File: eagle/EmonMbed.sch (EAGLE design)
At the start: 127 parts, among them IC2 74HC595D, IC3 74HC595D, IC4 ADE7758RW, J1 CON_TERMINAL_BLOCK_02-5MM, J2 CON_TERMINAL_BLOCK_02-5MM, J3 CON_TERMINAL_BLOCK_02-5MM, J4 CON_TERMINAL_BLOCK_03-5MM, J7 CON_TERMINAL_BLOCK_02-5MM, Q1 25MHz, U1 STM32L152RBT6, U2 W5500, Y1 32.768kHz, Y2 32.768kHz

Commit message: new schematics and datasheet
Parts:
- added C37: 10uF, rcl:CPOL-USC/6032-28R
- added C38, C39, C40, C41, C42, C43, C44, C55, C56: 0.1uF, rcl:C-USC0805
- added C45, C59: 10uF, rcl:CPOL-US153CLV-0605
- added C46, C60: 0.1uF, rcl:CPOL-US153CLV-0605
- added C47, C48, C49, C50, C51, C52, C53, C54: 100nF, rcl:C-EUC0603
- added D1, D2, D3, D4: 1N4001, diode:DIODE-DO-214AC
- added IC6: REG1117, burr-brown:REG1117
- added IC7: 7805DT, linear:7805DT
- added JP10, JP11: (no value), pinhead:PINHD-1X8
- added JP12, JP13: (no value), pinhead:PINHD-1X3
- added JP14: (no value), pinhead:PINHD-1X2
- added L1: 150Mhz, rcl:L-USWE-TPC
- added R41, R42: R120, resistor:R-EU_R0603
- added R43: 10, SparkFun-Passives:RESISTOR0603-RES
- added SV1: (no value), con-lstb:MA08-1
- added T3, T9: (no value), transistor-neu-to92:MMBT2222ALT1-NPN-SOT23-BEC
- added U$1, U$4: ADUM1402, adum140x:ADUM1402
- added U$3: ESP-07, esp-07:ESP-07
- added X2: (no value), con-ptr500:AK500/2-H
- C23, C24, C25, C26, C27, C28, C33, C34, C35, C36: device SparkFun-Passives:CAPPTH2 -> SparkFun-Passives:CAP0603-CAP
- JP1: value ESP8266 -> Vsel; device pinhead:PINHD-2X4 -> pinhead:PINHD-1X3
- R26, R27, R28, R29, R30, R31, R32, R33, R34, R35, R36, R37, R38: device SparkFun-Passives:RESISTORPTH-1/4W -> SparkFun-Passives:RESISTOR0603-RES
- R4: value 10k -> 10; device resistor:R-US_R0603 -> SparkFun-Passives:RESISTOR0603-RES
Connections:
- removed net CS: JP2.7
- removed net PA0: U1.PA0-WKUP1
- removed net PA1: U1.PA1
- removed net PA10: U1.PA10
- removed net PA11: U1.PA11
- removed net PA12: U1.PA12
- removed net PA15: U1.PA15
- removed net PA4: U1.PA4
- removed net PA8: U1.PA8
- removed net PA9: U1.PA9
- removed net PB0: U1.PB0
- removed net PB1: U1.PB1
- removed net PB12: U1.PB12
- removed net PB13: U1.PB13
- removed net PB14: U1.PB14
- removed net PB15: U1.PB15
- removed net PB4: U1.PB4
- removed net PB5: U1.PB5
- removed net PB7: U1.PB7
- removed net PC10: U1.PC10
- removed net PC11: U1.PC11
- removed net PC12: U1.PC12
- removed net PC4: U1.PC4
- removed net PC5: U1.PC5
- removed net PC6: U1.PC6
- removed net PC7: U1.PC7
- removed net PC8: U1.PC8
- removed net PC9: U1.PC9
- removed net PD2: U1.PD2
- removed net SCLK: U2.SCLK
- removed net SCSN: R8.1, U2.SCS_N
- removed net SDI(MOSI): JP2.4
- removed net SDO(MISO): JP2.1
- removed net SPI_CS: U1.PB6
- removed net SPI_MISO: U1.PA6
- removed net SPI_MOSI: U1.PA7
- removed net SPI_SCK: U1.PA5
- removed net TCK: U1.PA14
- removed net TMS: U1.PA13
- new net !CS: SV1.3
- new net ADE_CS: U$4.VIC, U1.PA12
- new net ADE_MISO: U$1.VOB, U1.PA14
- new net ADE_MOSI: U$1.VID, U1.PA15
- new net ADE_SCK: U$1.VIC, U1.PA13
- new net APCF: U$1.VOA, U1.PB4
- new net AVADE: C44.1, IC4.PWR.AVDD, R4.2
- new net DGND1: C51.2, C52.2
- new net ESP_GPIO0: JP13.2, U$3.GPIO0
- new net ESP_RX: JP14.1, U$3.URXD, U1.PC12
- new net ESP_TX: JP14.2, U$3.UTXD, U1.PD2
- new net ETH_CS: R8.1, U1.PA4, U2.SCS_N
- new net ETH_MISO: U1.PA6, U2.MISO
- new net ETH_MOSI: U1.PA7, U2.MOSI
- new net ETH_SCK: U1.PA5, U2.SCLK
- new net GESP: C54.2, JP12.2, JP13.3, U$3.GND, U$3.GPIO15
- new net GEXT: JP12.3
- new net IRQ: SV1.7, U$4.VOA, U1.PB6
- new net LCD_CS: JP2.7, U1.PB12
- new net LCD_MISO: JP2.1, U1.PB14
- new net LCD_MOSI: JP2.4, U1.PB15
- new net LCD_SCK: JP2.3, U1.PB13
- new net N$44: R41.2, T9.B
- new net N$45: R42.2, T3.B
- new net PWRKEY: R41.1
- new net VADE: C37.+, C38.1, C39.1, C40.1, C41.1, C42.1, C43.1, C60.+, D3.A, IC4.PWR.DVDD, IC7.VO, R4.1, U$1.VDD1, U$1.VDD2, U$1.VE1, U$1.VE2, U$4.VDD1, U$4.VDD2, U$4.VE1, U$4.VE2
- new net VARCF: U$4.VOB, U1.PB5
- new net VCC1: C51.1, C52.1
- new net VESP: C54.1, JP1.2, JP13.1, U$3.CH_PD, U$3.GPIO2, U$3.VCC
- new net VEXT: JP1.3
- new net VRAW: D1.A, D2.A, X2-1.KL
- net !ADECS: now also U$4.VOC
- net ADEAPCF: now also U$1.VIA
- net ADEIN: now also U$1.VOD
- net ADEIRQ: now also U$4.VIB
- net ADEOUT: now also U$1.VIB
- net ADESCK: now also U$1.VOC
- net ADEVARCF: now also U$4.VIA
- net AGND: now also C44.2, C47.2, C48.2, C49.2, C50.2, C56.2, L1.1
- net BOOT0: no longer R4.2
- net DGND: now also C37.-, C38.2, C39.2, C41.2, C43.2, C45.-, C46.-, C53.2, C55.2, C59.-, C60.-, IC6.GND, IC7.GND, JP12.1, L1.2, T3.E, T9.E, U$1.GND1@1, U$1.GND1@2, U$4.GND1@1, U$4.GND1@2, X2-2.KL; no longer JP1.2, R4.1
- net GND: now also C40.2, C42.2, SV1.2, U$1.GND2@1, U$1.GND2@2, U$4.GND2@1, U$4.GND2@2
- net MISO: now also SV1.6; no longer U2.MISO
- net MOSI: now also SV1.4; no longer U2.MOSI
- net Q1: now also JP10.1
- net Q10: now also JP11.2
- net Q11: now also JP11.3
- net Q12: now also JP11.4
- net Q13: now also JP11.5
- net Q14: now also JP11.6
- net Q15: now also JP11.7
- net Q16: now also JP11.8
- net Q2: now also JP10.2
- net Q3: now also JP10.3
- net Q4: now also JP10.4
- net Q5: now also JP10.5
- net Q6: now also JP10.6
- net Q7: now also JP10.7
- net Q8: now also JP10.8
- net Q9: now also JP11.1
- net RESET: now also R42.1
- net SCK: now also SV1.5; no longer JP2.3
- net SERIAL_RX: now also U1.PA10; no longer JP1.1, U1.PA3
- net SERIAL_TX: now also U1.PA9; no longer JP1.8, U1.PA2
- net SIM_PWRKEY: now also T9.C, U1.PC4
- net SIM_RESET: now also T3.C, U1.PC5
- net SIM_RX: now also U1.PC10
- net SIM_TX: now also U1.PC11
- net VCC: now also C47.1, C48.1, C49.1, C50.1, C56.1, R43.2, SV1.8; no longer IC4.PWR.AVDD
- net VDD: now also C46.+, C53.1, C55.1, D4.A, IC6.VOUT, JP1.1, R43.1; no longer IC4.PWR.DVDD, JP1.3, JP1.7
- net VIN: now also C45.+, C59.+, D1.C, D2.C, D3.C, D4.C, IC6.VIN, IC7.VI
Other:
- note added: "LMS8117A"
- moved on the sheet: C1, C10, C10-4U7, C11, C11-22P, C12, C13, C14, C15, C16, C17, C18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

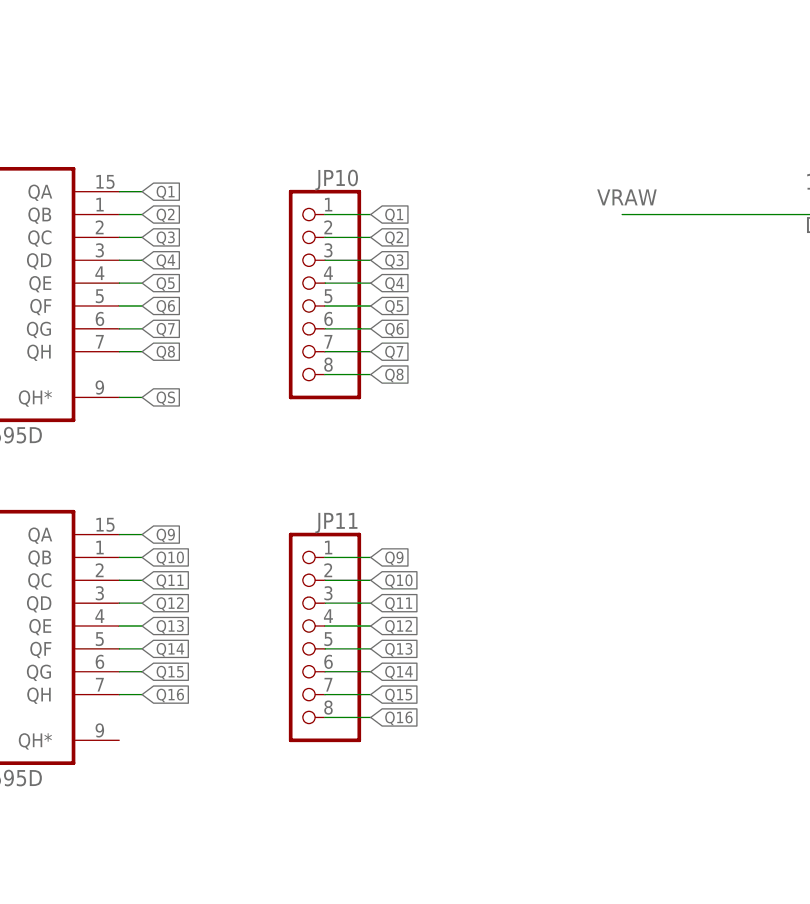
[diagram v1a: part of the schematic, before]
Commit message: update schematic
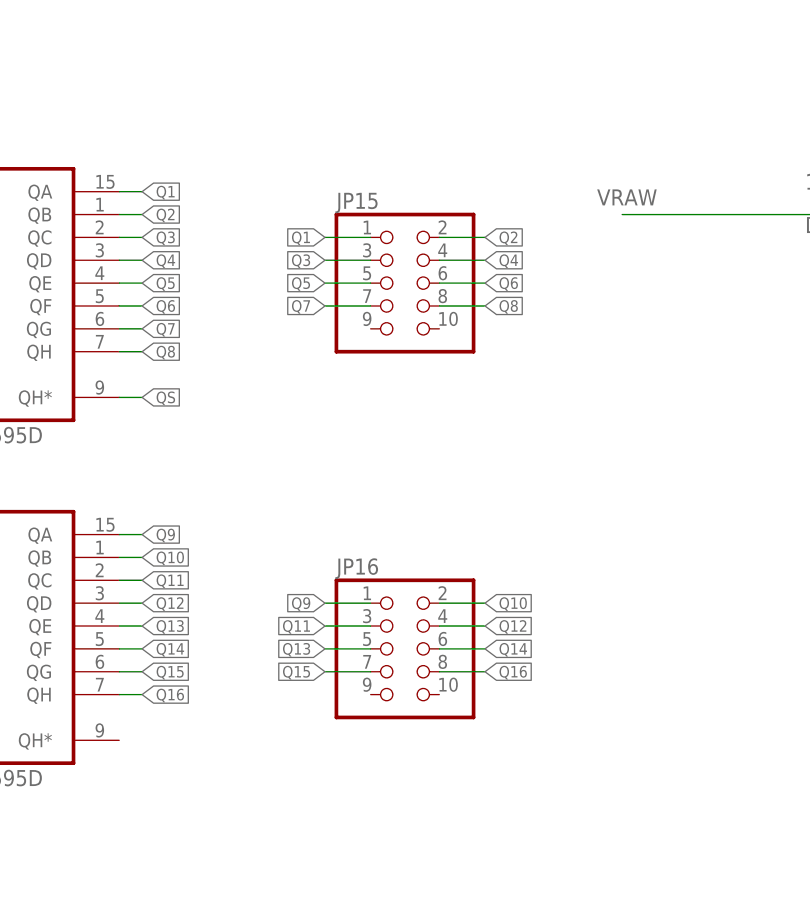
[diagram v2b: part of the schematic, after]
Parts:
- removed JP10, JP11: (no value), pinhead:PINHD-1X8
- added JP15, JP16: (no value), pinhead:PINHD-2X5/90
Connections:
- net Q1: now also JP15.1; no longer JP10.1
- net Q10: now also JP16.2; no longer JP11.2
- net Q11: now also JP16.3; no longer JP11.3
- net Q12: now also JP16.4; no longer JP11.4
- net Q13: now also JP16.5; no longer JP11.5
- net Q14: now also JP16.6; no longer JP11.6
- net Q15: now also JP16.7; no longer JP11.7
- net Q16: now also JP16.8; no longer JP11.8
- net Q2: now also JP15.2; no longer JP10.2
- net Q3: now also JP15.3; no longer JP10.3
- net Q4: now also JP15.4; no longer JP10.4
- net Q5: now also JP15.5; no longer JP10.5
- net Q6: now also JP15.6; no longer JP10.6
- net Q7: now also JP15.7; no longer JP10.7
- net Q8: now also JP15.8; no longer JP10.8
- net Q9: now also JP16.1; no longer JP11.1
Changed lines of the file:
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@@
 <part name="R40" library="resistor" deviceset="R-US_" device="R0603" value="10k"/>
 <part name="JP9" library="pinhead" deviceset="PINHD-1X4" device="" value="USART"/>
-<part name="JP10" library="pinhead" deviceset="PINHD-1X8" device=""/>
-<part name="JP11" library="pinhead" deviceset="PINHD-1X8" device=""/>
 <part name="U$3" library="esp-07" deviceset="ESP-07" device=""/>
 <part name="JP1" library="pinhead" deviceset="PINHD-1X3" device="" value="Vsel"/>
@@
 <part name="C45" library="rcl" deviceset="CPOL-US" device="153CLV-0605" value="10uF"/>
 <part name="C46" library="rcl" deviceset="CPOL-US" device="153CLV-0605" value="0.1uF"/>
+<part name="JP15" library="pinhead" deviceset="PINHD-2X5" device="/90"/>
+<part name="JP16" library="pinhead" deviceset="PINHD-2X5" device="/90"/>
 </parts>
 <sheets>
@@
 <instance part="R40" gate="G$1" x="132.08" y="187.96"/>
 <instance part="JP9" gate="A" x="177.8" y="160.02"/>
-<instance part="JP10" gate="A" x="408.94" y="269.24" rot="MR0"/>
-<instance part="JP11" gate="A" x="408.94" y="231.14" rot="MR0"/>
 <instance part="U$3" gate="G$1" x="386.08" y="330.2"/>
 <instance part="JP1" gate="A" x="396.24" y="373.38"/>
@@
 <instance part="C45" gate="G$1" x="477.52" y="271.78"/>
 <instance part="C46" gate="G$1" x="505.46" y="271.78"/>
+<instance part="JP15" gate="A" x="419.1" y="271.78"/>
+<instance part="JP16" gate="A" x="419.1" y="231.14"/>
 </instances>
 <busses>
@@
 </segment>
 <segment>
-<pinref part="JP10" gate="A" pin="8"/>
-<wire x1="416.56" y1="261.62" x2="411.48" y2="261.62" width="0.1524" layer="91"/>
-<label x="416.56" y="261.62" size="1.27" layer="95" xref="yes"/>
+<pinref part="JP15" gate="A" pin="8"/>
+<wire x1="424.18" y1="269.24" x2="429.26" y2="269.24" width="0.1524" layer="91"/>
+<label x="429.26" y="269.24" size="1.27" layer="95" xref="yes"/>
 </segment>
 </net>
@@
 </segment>
 <segment>
-<pinref part="JP10" gate="A" pin="7"/>
-<wire x1="411.48" y1="264.16" x2="416.56" y2="264.16" width="0.1524" layer="91"/>
-<label x="416.56" y="264.16" size="1.27" layer="95" xref="yes"/>
+<pinref part="JP15" gate="A" pin="7"/>
+<wire x1="416.56" y1="269.24" x2="411.48" y2="269.24" width="0.1524" layer="91"/>
+<label x="411.48" y="269.24" size="1.27" layer="95" rot="R180" xref="yes"/>
 </segment>
 </net>
@@
 </segment>
 <segment>
-<pinref part="JP10" gate="A" pin="6"/>
-<wire x1="416.56" y1="266.7" x2="411.48" y2="266.7" width="0.1524" layer="91"/>
-<label x="416.56" y="266.7" size="1.27" layer="95" xref="yes"/>
+<pinref part="JP15" gate="A" pin="6"/>
+<wire x1="429.26" y1="271.78" x2="424.18" y2="271.78" width="0.1524" layer="91"/>
+<label x="429.26" y="271.78" size="1.27" layer="95" xref="yes"/>
 </segment>
 </net>
@@
 </segment>
 <segment>
-<pinref part="JP10" gate="A" pin="5"/>
-<wire x1="411.48" y1="269.24" x2="416.56" y2="269.24" width="0.1524" layer="91"/>
-<label x="416.56" y="269.24" size="1.27" layer="95" xref="yes"/>
+<pinref part="JP15" gate="A" pin="5"/>
+<wire x1="416.56" y1="271.78" x2="411.48" y2="271.78" width="0.1524" layer="91"/>
+<label x="411.48" y="271.78" size="1.27" layer="95" rot="R180" xref="yes"/>
 </segment>
 </net>
@@
 </segment>
 <segment>
-<pinref part="JP10" gate="A" pin="4"/>
-<wire x1="416.56" y1="271.78" x2="411.48" y2="271.78" width="0.1524" layer="91"/>
-<label x="416.56" y="271.78" size="1.27" layer="95" xref="yes"/>
+<pinref part="JP15" gate="A" pin="4"/>
+<wire x1="424.18" y1="274.32" x2="429.26" y2="274.32" width="0.1524" layer="91"/>
+<label x="429.26" y="274.32" size="1.27" layer="95" xref="yes"/>
 </segment>
 </net>
@@
 </segment>
 <segment>
-<pinref part="JP10" gate="A" pin="3"/>
-<wire x1="411.48" y1="274.32" x2="416.56" y2="274.32" width="0.1524" layer="91"/>
-<label x="416.56" y="274.32" size="1.27" layer="95" xref="yes"/>
+<pinref part="JP15" gate="A" pin="3"/>
+<wire x1="416.56" y1="274.32" x2="411.48" y2="274.32" width="0.1524" layer="91"/>
+<label x="411.48" y="274.32" size="1.27" layer="95" rot="R180" xref="yes"/>
 </segment>
 </net>
@@
 </segment>
 <segment>
-<pinref part="JP10" gate="A" pin="2"/>
-<wire x1="416.56" y1="276.86" x2="411.48" y2="276.86" width="0.1524" layer="91"/>
-<label x="416.56" y="276.86" size="1.27" layer="95" xref="yes"/>
+<pinref part="JP15" gate="A" pin="2"/>
+<wire x1="424.18" y1="276.86" x2="429.26" y2="276.86" width="0.1524" layer="91"/>
+<label x="429.26" y="276.86" size="1.27" layer="95" xref="yes"/>
 </segment>
 </net>
@@
 </segment>
 <segment>
-<pinref part="JP10" gate="A" pin="1"/>
-<wire x1="411.48" y1="279.4" x2="416.56" y2="279.4" width="0.1524" layer="91"/>
-<label x="416.56" y="279.4" size="1.27" layer="95" xref="yes"/>
+<pinref part="JP15" gate="A" pin="1"/>
+<wire x1="416.56" y1="276.86" x2="411.48" y2="276.86" width="0.1524" layer="91"/>
+<label x="411.48" y="276.86" size="1.27" layer="95" rot="R180" xref="yes"/>
 </segment>
 </net>
@@
 </segment>
 <segment>
-<pinref part="JP11" gate="A" pin="8"/>
-<wire x1="416.56" y1="223.52" x2="411.48" y2="223.52" width="0.1524" layer="91"/>
-<label x="416.56" y="223.52" size="1.27" layer="95" xref="yes"/>
+<pinref part="JP16" gate="A" pin="8"/>
+<wire x1="429.26" y1="228.6" x2="424.18" y2="228.6" width="0.1524" layer="91"/>
+<label x="429.26" y="228.6" size="1.27" layer="95" xref="yes"/>
 </segment>
 </net>
@@
 </segment>
 <segment>
-<pinref part="JP11" gate="A" pin="7"/>
-<wire x1="411.48" y1="226.06" x2="416.56" y2="226.06" width="0.1524" layer="91"/>
-<label x="416.56" y="226.06" size="1.27" layer="95" xref="yes"/>
+<pinref part="JP16" gate="A" pin="7"/>
+<wire x1="411.48" y1="228.6" x2="416.56" y2="228.6" width="0.1524" layer="91"/>
+<label x="411.48" y="228.6" size="1.27" layer="95" rot="R180" xref="yes"/>
 </segment>
 </net>
@@
 </segment>
 <segment>
-<pinref part="JP11" gate="A" pin="6"/>
-<wire x1="416.56" y1="228.6" x2="411.48" y2="228.6" width="0.1524" layer="91"/>
-<label x="416.56" y="228.6" size="1.27" layer="95" xref="yes"/>
+<pinref part="JP16" gate="A" pin="6"/>
+<wire x1="424.18" y1="231.14" x2="429.26" y2="231.14" width="0.1524" layer="91"/>
+<label x="429.26" y="231.14" size="1.27" layer="95" xref="yes"/>
 </segment>
 </net>
@@
 </segment>
 <segment>
-<pinref part="JP11" gate="A" pin="5"/>
-<wire x1="411.48" y1="231.14" x2="416.56" y2="231.14" width="0.1524" layer="91"/>
-<label x="416.56" y="231.14" size="1.27" layer="95" xref="yes"/>
+<pinref part="JP16" gate="A" pin="5"/>
+<wire x1="416.56" y1="231.14" x2="411.48" y2="231.14" width="0.1524" layer="91"/>
+<label x="411.48" y="231.14" size="1.27" layer="95" rot="R180" xref="yes"/>
 </segment>
 </net>
@@
 </segment>
 <segment>
-<pinref part="JP11" gate="A" pin="4"/>
-<wire x1="416.56" y1="233.68" x2="411.48" y2="233.68" width="0.1524" layer="91"/>
-<label x="416.56" y="233.68" size="1.27" layer="95" xref="yes"/>
+<pinref part="JP16" gate="A" pin="4"/>
+<wire x1="429.26" y1="233.68" x2="424.18" y2="233.68" width="0.1524" layer="91"/>
+<label x="429.26" y="233.68" size="1.27" layer="95" xref="yes"/>
 </segment>
 </net>
@@
 </segment>
 <segment>
-<pinref part="JP11" gate="A" pin="3"/>
-<wire x1="411.48" y1="236.22" x2="416.56" y2="236.22" width="0.1524" layer="91"/>
-<label x="416.56" y="236.22" size="1.27" layer="95" xref="yes"/>
+<pinref part="JP16" gate="A" pin="3"/>
+<wire x1="411.48" y1="233.68" x2="416.56" y2="233.68" width="0.1524" layer="91"/>
+<label x="411.48" y="233.68" size="1.27" layer="95" rot="R180" xref="yes"/>
 </segment>
 </net>
@@
 </segment>
 <segment>
-<pinref part="JP11" gate="A" pin="2"/>
-<wire x1="416.56" y1="238.76" x2="411.48" y2="238.76" width="0.1524" layer="91"/>
-<label x="416.56" y="238.76" size="1.27" layer="95" xref="yes"/>
+<pinref part="JP16" gate="A" pin="2"/>
+<wire x1="424.18" y1="236.22" x2="429.26" y2="236.22" width="0.1524" layer="91"/>
+<label x="429.26" y="236.22" size="1.27" layer="95" xref="yes"/>
 </segment>
 </net>
@@
 </segment>
 <segment>
-<pinref part="JP11" gate="A" pin="1"/>
-<wire x1="411.48" y1="241.3" x2="416.56" y2="241.3" width="0.1524" layer="91"/>
-<label x="416.56" y="241.3" size="1.27" layer="95" xref="yes"/>
-</segment>
-</net>
+<pinref part="JP16" gate="A" pin="1"/>
+<wire x1="416.56" y1="236.22" x2="411.48" y2="236.22" width="0.1524" layer="91"/>
+<label x="411.48" y="236.22" size="1.27" layer="95" rot="R180" xref="yes"/>
+</segment>
+</net>
